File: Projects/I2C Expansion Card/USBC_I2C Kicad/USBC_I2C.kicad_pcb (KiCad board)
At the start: 2 copper layers, 26 x 30 mm, 21 parts, among them U1 MCP2221A

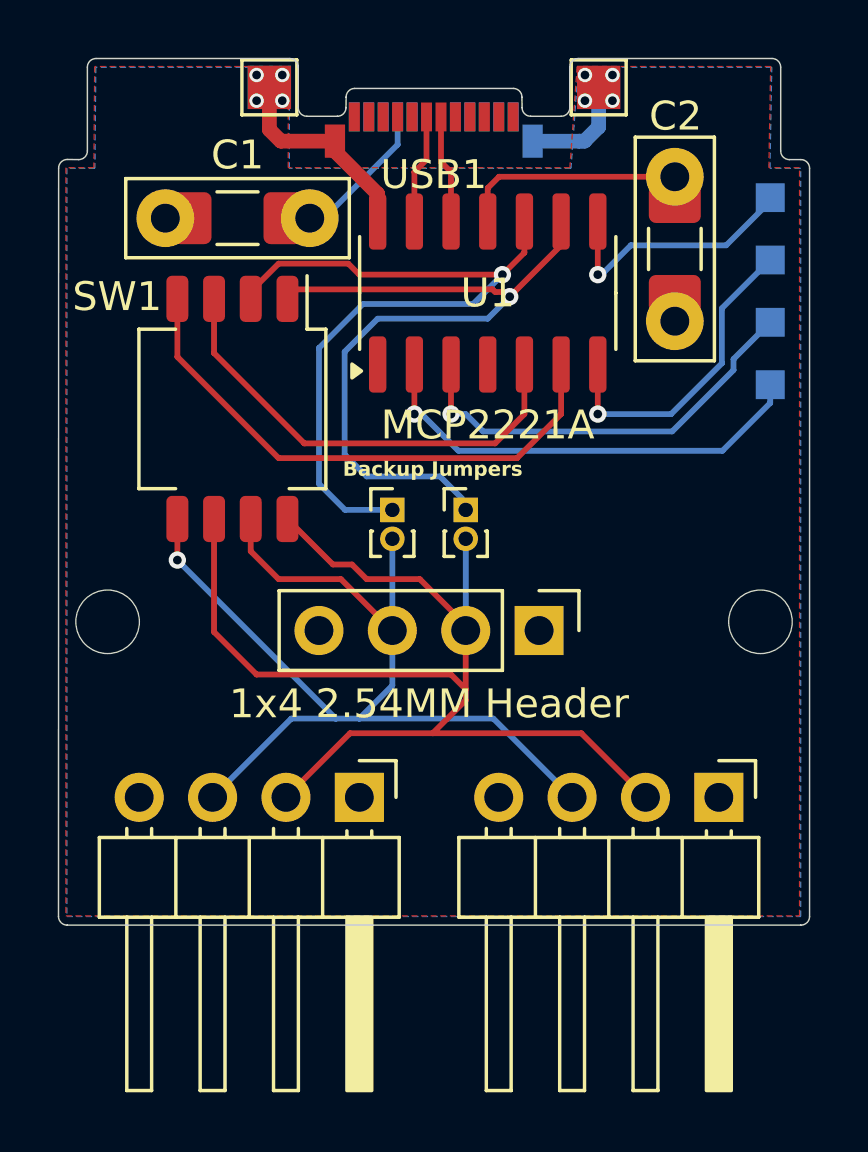
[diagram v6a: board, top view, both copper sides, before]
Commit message: Moved a few traces and fixed edge
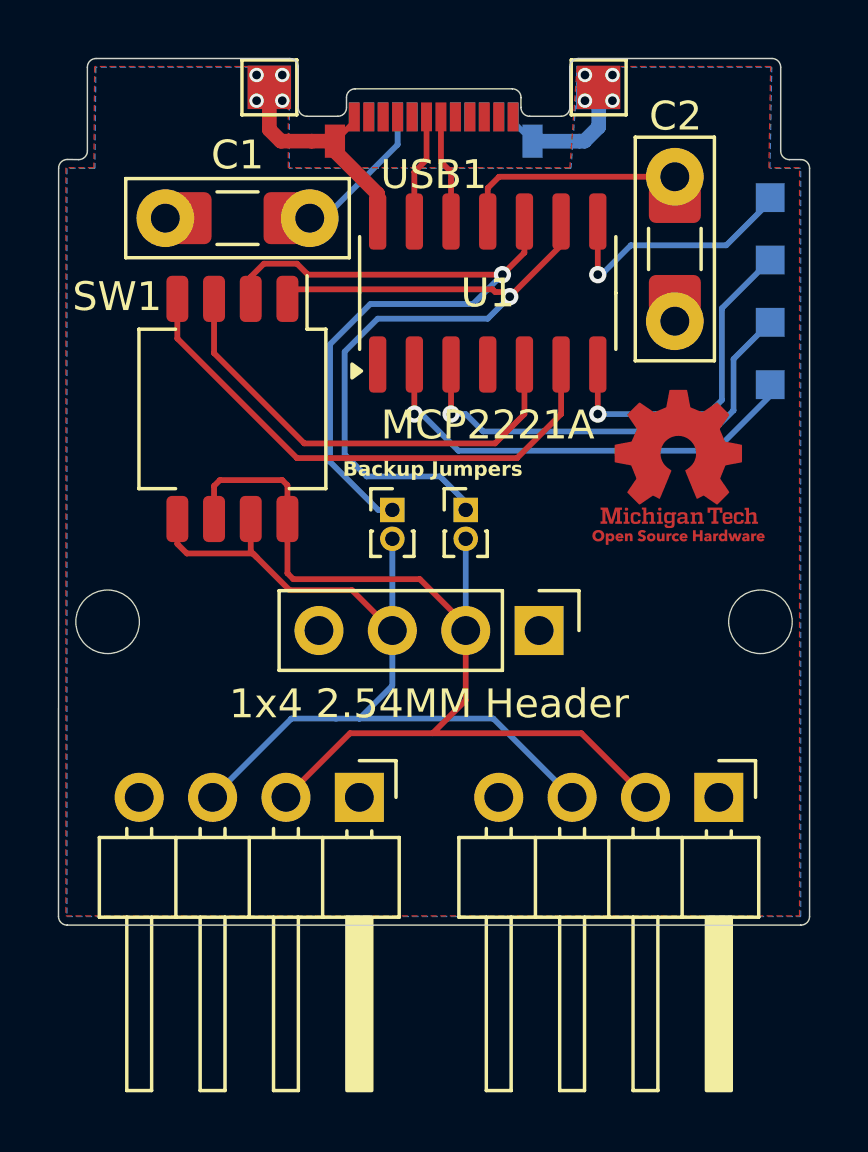
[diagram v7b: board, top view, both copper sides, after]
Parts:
- added G***: LOGO, LOGO, F.Cu at (105.3, 71.4)
- added TP2: TestPoint, TestPoint:TestPoint_Pad_1.5x1.5mm, B.Cu at (102.5, 58.2)
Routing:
- net (no net): track 80.2 -> 67.5 mm, vias 1 -> 0
- net GND: track 12.3 -> 14.6 mm
- net SCL: track 26.7 -> 25.9 mm
- net Net-(D2-A): track 14.9 -> 15.7 mm
- net Net-(D3-A): track 11.0 -> 11.8 mm
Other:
- outline, holes or cut-outs redrawn
